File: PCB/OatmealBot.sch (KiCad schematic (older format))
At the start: 32 parts, among them J1 TerminalBlock_5pin_3.5mm, J10 ServoHeader3, J2 RPi_GPIO, J3 TerminalBlock_5pin_3.5mm, J4 ServoHeader1, J5 Motor 3, J6 Motor 4, J7 ServoHeader2, J8 Motor 1, J9 Motor 2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

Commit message: Created symbol for TB6612FNG motor driver. Added first motor driver and hooked it up.
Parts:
- removed J1, J3: TerminalBlock_5pin_3.5mm, symbol TerminalBlock_5pin_3.5mm
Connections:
- wire segments 176 -> 191
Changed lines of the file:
@@
-	-1   0    0    -1
-$EndComp
-$Comp
-L TerminalBlock_5pin_3.5mm J1
-U 1 1 5B1F55DC
-P 1000 2050
-F 0 "J1" H 1000 1750 60  0000 C CNN
-F 1 "TerminalBlock_5pin_3.5mm" H 1000 1650 60  0000 C CNN
-F 2 "" H 1000 2050 60  0001 C CNN
-F 3 "" H 1000 2050 60  0001 C CNN
-	1    1000 2050
-	0    1    1    0
-$EndComp
-$Comp
-L GND #PWR01
-U 1 1 5B1F569E
-P 1600 2050
-F 0 "#PWR01" H 1600 1800 50  0001 C CNN
-F 1 "GND" H 1600 1900 50  0000 C CNN
-F 2 "" H 1600 2050 50  0000 C CNN
-F 3 "" H 1600 2050 50  0000 C CNN
-	1    1600 2050
 	-1   0    0    -1
 $EndComp
@@
 	-1   0    0    -1
 $EndComp
-Text GLabel 1600 2750 0    60   Input ~ 0
+Text GLabel 1700 2750 0    60   Input ~ 0
 +5V
 $Comp
@@
 	1750 2600 1650 2600
 Wire Wire Line
-	1750 2750 1600 2750
-Wire Wire Line
-	1200 2050 1600 2050
-Wire Wire Line
-	1200 1850 1200 1100
-Wire Wire Line
-	1200 1100 1750 1100
-Wire Wire Line
-	1200 1950 1300 1950
-Wire Wire Line
-	1300 1950 1300 1250
-Wire Wire Line
-	1300 1250 1750 1250
-Wire Wire Line
-	1200 2150 1400 2150
-Wire Wire Line
-	1400 2150 1400 2300
-Wire Wire Line
-	1400 2300 1750 2300
-Wire Wire Line
-	1200 2250 1300 2250
-Wire Wire Line
-	1300 2250 1300 2450
-Wire Wire Line
-	1300 2450 1750 2450
-$Comp
-L TerminalBlock_5pin_3.5mm J3
-U 1 1 5B2052F2
-P 1000 4650
-F 0 "J3" H 1000 4350 60  0000 C CNN
-F 1 "TerminalBlock_5pin_3.5mm" H 1000 4250 60  0000 C CNN
-F 2 "" H 1000 4650 60  0001 C CNN
-F 3 "" H 1000 4650 60  0001 C CNN
-	1    1000 4650
-	0    1    1    0
-$EndComp
-Wire Wire Line
-	1200 4450 1200 3750
+	1750 2750 1700 2750
+Wire Wire Line
+	1100 1100 1750 1100
+Wire Wire Line
+	1200 1250 1750 1250
+Wire Wire Line
+	1300 2300 1750 2300
 Wire Wire Line
 	1200 3750 1700 3750
 Wire Wire Line
-	1200 4550 1300 4550
-Wire Wire Line
-	1300 4550 1300 3900
-Wire Wire Line
 	1300 3900 1700 3900
-$Comp
-L GND #PWR04
-U 1 1 5B20544B
-P 1400 4650
-F 0 "#PWR04" H 1400 4400 50  0001 C CNN
-F 1 "GND" H 1400 4500 50  0000 C CNN
-F 2 "" H 1400 4650 50  0000 C CNN
-F 3 "" H 1400 4650 50  0000 C CNN
-	1    1400 4650
-	1    0    0    -1
-$EndComp
 $Comp
 L GND #PWR05
@@
 	1700 4050 1600 4050
 Wire Wire Line
-	1200 4650 1400 4650
-Wire Wire Line
 	1600 5300 1700 5300
 Text GLabel 1550 5450 0    60   Input ~ 0
@@
 	1700 5450 1550 5450
 Wire Wire Line
-	1200 4750 1300 4750
-Wire Wire Line
-	1300 4750 1300 5000
-Wire Wire Line
 	1300 5000 1700 5000
-Wire Wire Line
-	1200 4850 1200 5150
 Wire Wire Line
 	1200 5150 1700 5150
@@
 	4000 2650 4000 2550
 Wire Wire Line
-	3850 2550 4250 2550
+	3850 2550 4000 2550
+Wire Wire Line
+	4000 2550 4250 2550
 Wire Wire Line
 	3850 2650 3850 2550
 Connection ~ 4000 2550
 Wire Wire Line
-	3500 2350 3500 2650
+	3500 2350 3500 2550
+Wire Wire Line
+	3500 2550 3500 2650
 Wire Wire Line
 	3650 2650 3650 2550
@@
 	1700 4500 1700 4650
 Wire Wire Line
-	1700 4650 3000 4650
-Wire Wire Line
-	3000 4650 3000 3550
-Wire Wire Line
-	3000 3550 3250 3550
+	1700 4650 2950 4650
+Wire Wire Line
+	2950 4650 2950 3550
+Wire Wire Line
+	2950 3550 3250 3550
 Wire Wire Line
 	1700 4350 1600 4350
@@
 	1600 4350 1600 4750
 Wire Wire Line
-	1600 4750 3100 4750
-Wire Wire Line
-	3100 4750 3100 3650
-Wire Wire Line
-	3100 3650 3250 3650
+	1600 4750 3050 4750
+Wire Wire Line
+	3050 4750 3050 3650
+Wire Wire Line
+	3050 3650 3250 3650
 Wire Wire Line
 	3150 6000 3150 3750
@@
 	1050 7150 1050 6550
 Wire Wire Line
-	600  6550 5550 6550
+	600  6550 1050 6550
+Wire Wire Line
+	1050 6550 1800 6550
+Wire Wire Line
+	1800 6550 2550 6550
+Wire Wire Line
+	2550 6550 3300 6550
+Wire Wire Line
+	3300 6550 4050 6550
+Wire Wire Line
+	4050 6550 4800 6550
+Wire Wire Line
+	4800 6550 5550 6550
 Wire Wire Line
 	1800 6550 1800 7150
@@
 +5V
 Wire Wire Line
-	1250 6250 1250 7150
-Wire Wire Line
-	1250 6400 5750 6400
+	1250 6250 1250 6400
+Wire Wire Line
+	1250 6400 1250 7150
+Wire Wire Line
+	1250 6400 2000 6400
+Wire Wire Line
+	2000 6400 2750 6400
+Wire Wire Line
+	2750 6400 3500 6400
+Wire Wire Line
+	3500 6400 4250 6400
+Wire Wire Line
+	4250 6400 5000 6400
+Wire Wire Line
+	5000 6400 5750 6400
 Wire Wire Line
 	2000 6400 2000 7150
@@
 	7900 2650 8000 2650
 Wire Wire Line
-	8000 2450 8000 2750
+	8000 2450 8000 2650
+Wire Wire Line
+	8000 2650 8000 2750
 Wire Wire Line
 	8000 2750 7900 2750
@@
 $EndComp
 Wire Wire Line
-	4650 1900 4650 2100
-Wire Wire Line
-	3900 1700 4350 1700
-Wire Wire Line
-	4100 2000 4950 2000
+	4650 1900 4650 2000
+Wire Wire Line
+	4650 2000 4650 2100
+Wire Wire Line
+	3900 1700 4100 1700
+Wire Wire Line
+	4100 1700 4350 1700
+Wire Wire Line
+	4100 2000 4650 2000
+Wire Wire Line
+	4650 2000 4950 2000
 Connection ~ 4650 2000
 Text GLabel 5850 2950 0    60   Output ~ 0
@@
 $EndComp
 Wire Wire Line
-	4600 1000 4600 1200
-Wire Wire Line
-	4100 1100 4900 1100
+	4600 1000 4600 1100
+Wire Wire Line
+	4600 1100 4600 1200
+Wire Wire Line
+	4100 1100 4600 1100
+Wire Wire Line
+	4600 1100 4900 1100
 Connection ~ 4600 1100
 Wire Wire Line
@@
 	4900 600  4600 600
 Wire Wire Line
-	3900 800  4300 800
+	3900 800  4100 800
+Wire Wire Line
+	4100 800  4300 800
 Text GLabel 3900 800  0    60   Input ~ 0
 HighPower2
@@
 	6000 2850 5850 2850
 Wire Wire Line
-	8650 6250 8950 6250
+	8650 6250 8800 6250
+Wire Wire Line
+	8800 6250 8950 6250
 Wire Wire Line
 	8800 6100 8800 6250
@@
 	5200 7150 5200 7000
 $Sheet
-S 3900 5050 1250 500
+S 550  2600 500  1750
 U 5B4A79AB
 F0 "MotorController" 60
 F1 "OatmealBoxMotorController.sch" 60
+F2 "Motor1+" I R 1050 2700 60
+F3 "Motor1-" I R 1050 2850 60
+F4 "Motor2+" I R 1050 3000 60
+F5 "Motor2-" I R 1050 3150 60
 $EndSheet
+Wire Wire Line
+	1050 2700 1100 2700
+Wire Wire Line
+	1100 2700 1100 1100
+Wire Wire Line
+	1200 1250 1200 2850
+Wire Wire Line
+	1200 2850 1050 2850
+Wire Wire Line
+	1300 2300 1300 3000
+Wire Wire Line
+	1300 3000 1050 3000
+Wire Wire Line
+	1750 2450 1400 2450
+Wire Wire Line
+	1400 2450 1400 3150
+Wire Wire Line
+	1400 3150 1050 3150
 $EndSCHEMATC

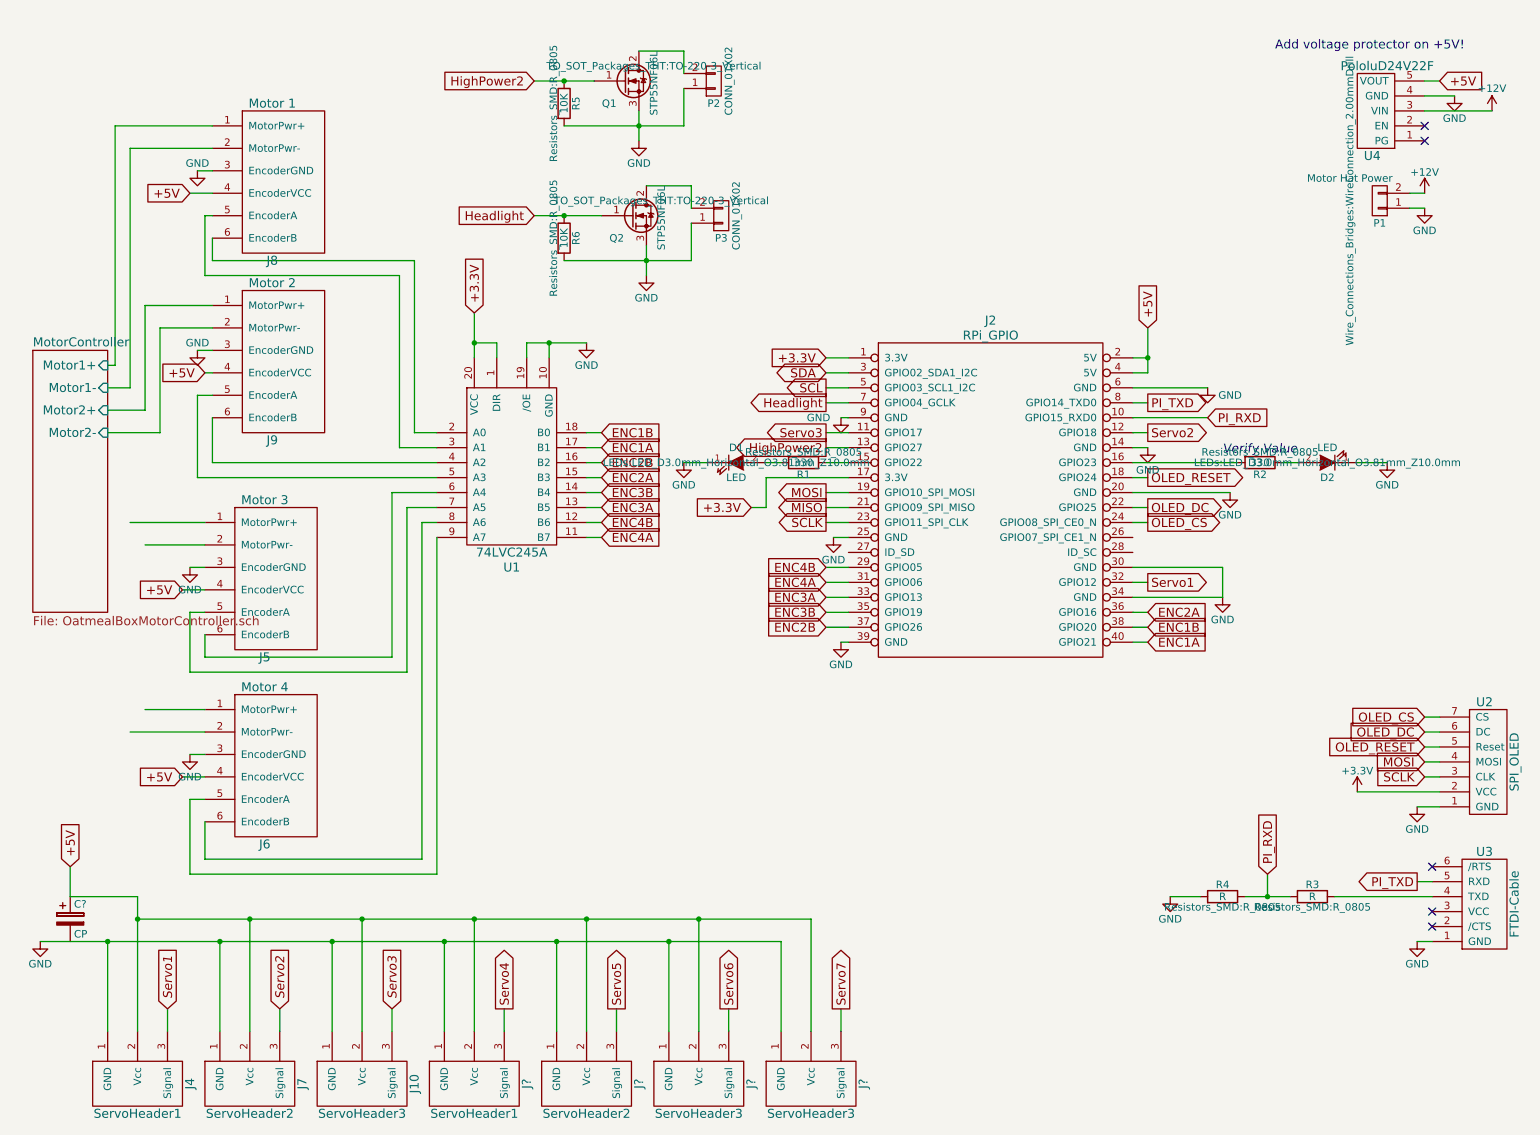
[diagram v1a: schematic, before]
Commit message: Added second motor driver. Got everything hooked up back.
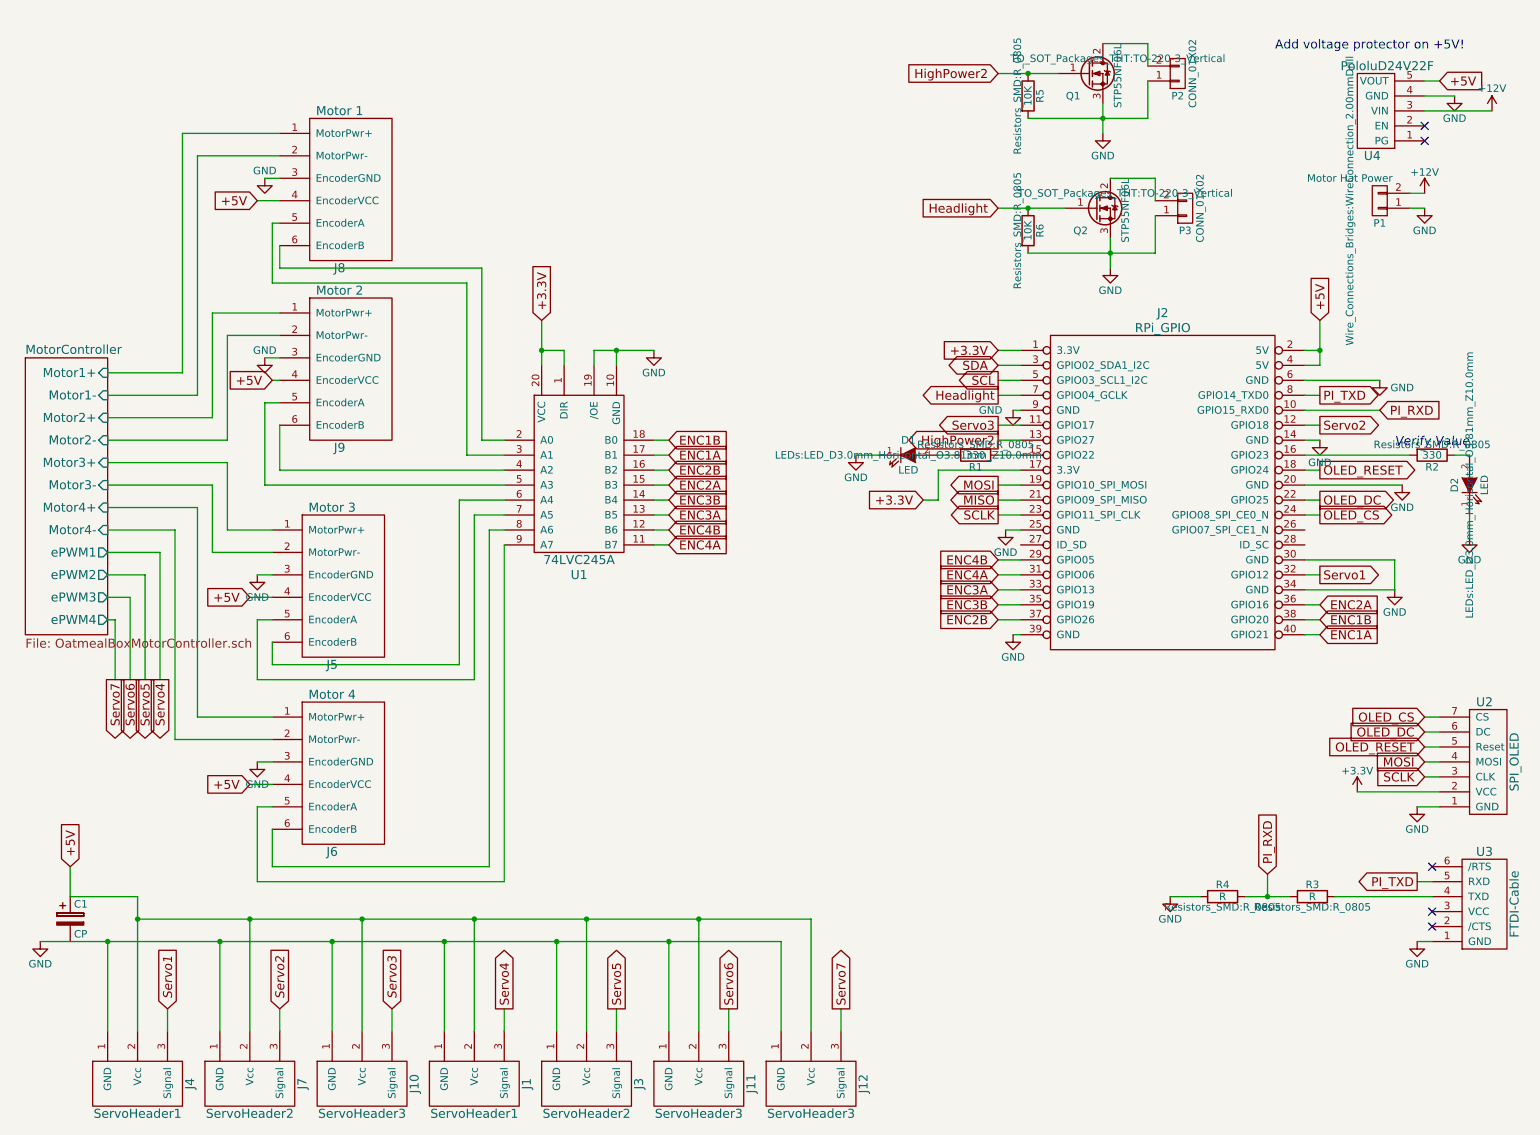
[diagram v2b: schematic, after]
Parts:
- gave numbers to parts that had none: 5
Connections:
- net MotorController/Motor3+: now reaches J5.1 (MotorPwr+)
- net MotorController/Motor3-: now reaches J5.2 (MotorPwr-)
- net MotorController/Motor4+: now reaches J6.1 (MotorPwr+)
- net MotorController/Motor4-: now reaches J6.2 (MotorPwr-)
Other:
- moved on the sheet: D1, D2, J2, J5, J6, J8, J9, P2, P3, Q1, Q2, R1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

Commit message: Connected I2C, fixed ERC errors
Connected I2C to the PWM controller.
Fixed ERC errors.
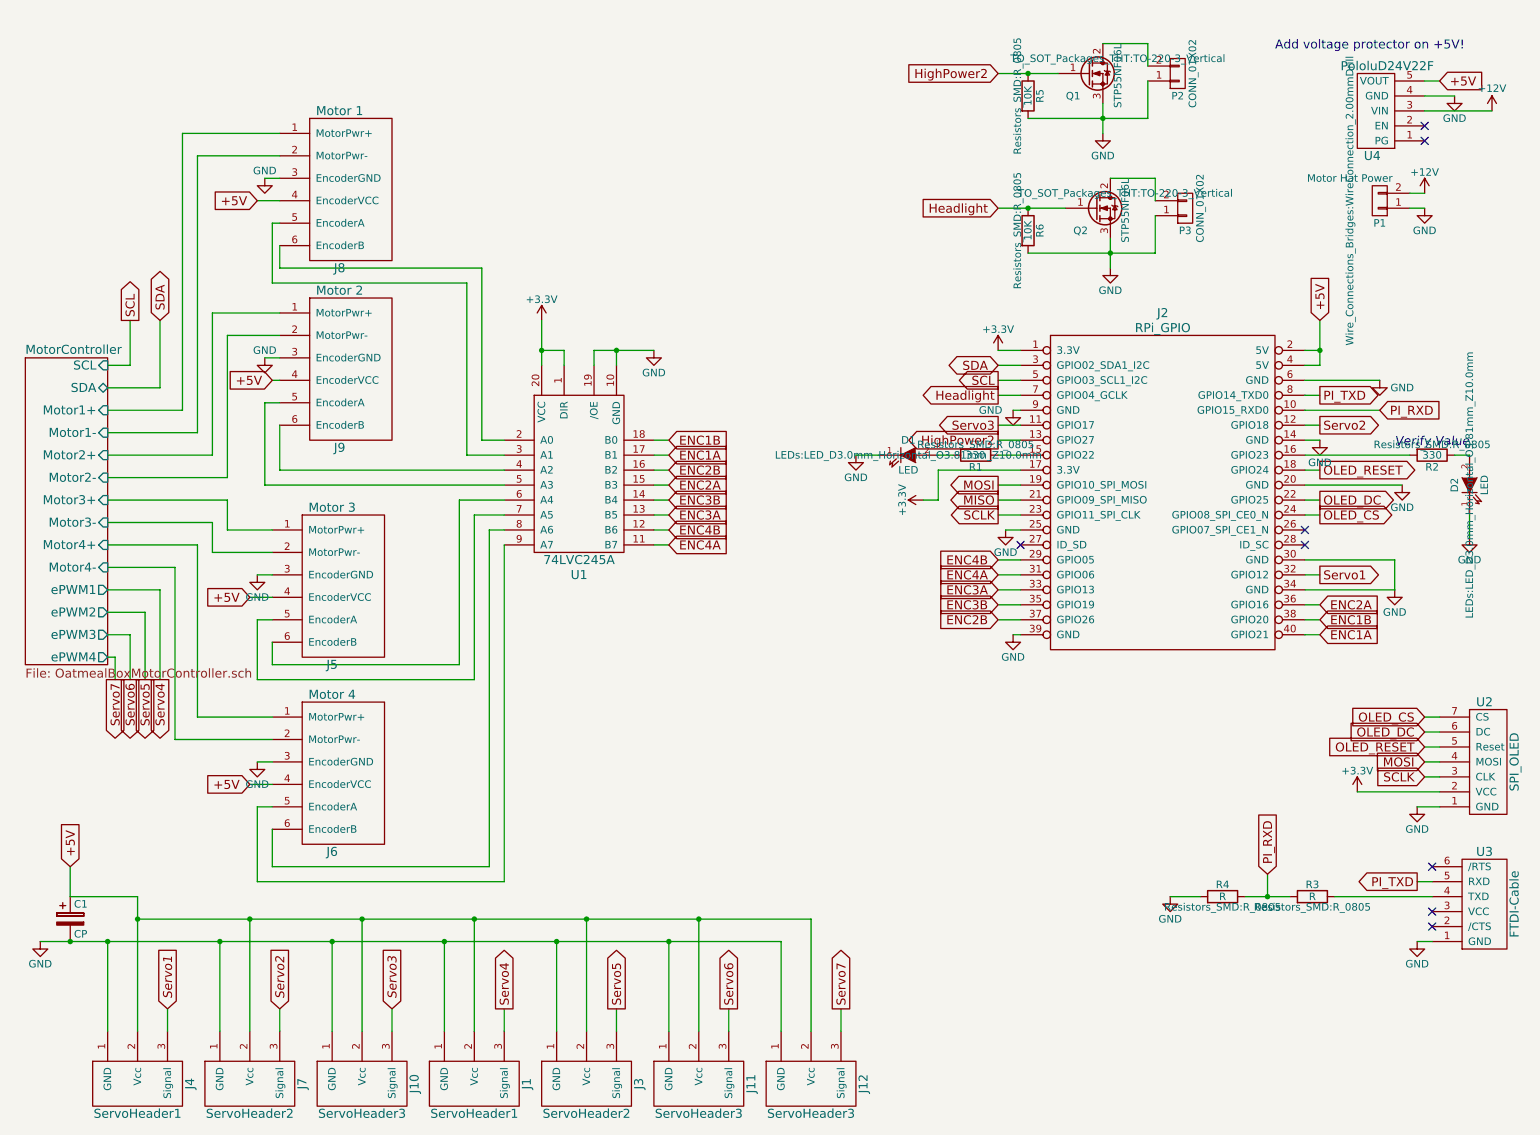
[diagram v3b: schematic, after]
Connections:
- net +3.3V is gone; now on net +3V3: J2.1 (3.3V), J2.17 (3.3V), U1.1 (DIR), U1.20 (VCC)
- net GND: now also C1.2
- no-connect marks 5 -> 8
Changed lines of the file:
@@
 	1    0    0    -1
 $EndComp
-Text GLabel 3950 2400 1    60   Input ~ 0
-+3.3V
 $Comp
 L GND #PWR05
@@
 Wire Wire Line
 	9150 3700 9050 3700
-Text GLabel 7000 2600 0    60   Input ~ 0
-+3.3V
 Wire Wire Line
 	7150 2600 7000 2600
@@
 	7150 3200 7000 3200
 Connection ~ 7200 750
-Text GLabel 6500 3600 0    60   Input ~ 0
-+3.3V
 Wire Wire Line
 	7150 3400 6600 3400
@@
 	5200 7150 5200 7000
 $Sheet
-S 500  2650 550  1850
+S 500  2650 550  2050
 U 5B4A79AB
 F0 "MotorController" 60
 F1 "OatmealBoxMotorController.sch" 60
-F2 "Motor1+" I R 1050 2750 60
-F3 "Motor1-" I R 1050 2900 60
-F4 "Motor2+" I R 1050 3050 60
-F5 "Motor2-" I R 1050 3200 60
-F6 "Motor3+" I R 1050 3350 60
-F7 "Motor3-" I R 1050 3500 60
-F8 "Motor4+" I R 1050 3650 60
-F9 "Motor4-" I R 1050 3800 60
-F10 "ePWM1" O R 1050 3950 60
-F11 "ePWM2" O R 1050 4100 60
-F12 "ePWM3" O R 1050 4250 60
-F13 "ePWM4" O R 1050 4400 60
+F2 "Motor1+" I R 1050 3000 60
+F3 "Motor1-" I R 1050 3150 60
+F4 "Motor2+" I R 1050 3300 60
+F5 "Motor2-" I R 1050 3450 60
+F6 "Motor3+" I R 1050 3600 60
+F7 "Motor3-" I R 1050 3750 60
+F8 "Motor4+" I R 1050 3900 60
+F9 "Motor4-" I R 1050 4050 60
+F10 "ePWM1" O R 1050 4200 60
+F11 "ePWM2" O R 1050 4350 60
+F12 "ePWM3" O R 1050 4500 60
+F13 "ePWM4" O R 1050 4650 60
+F14 "SDA" B R 1050 2850 60
+F15 "SCL" I R 1050 2700 60
 $EndSheet
 Wire Wire Line
-	1650 1300 1650 2900
-Wire Wire Line
-	1650 2900 1050 2900
-Wire Wire Line
-	1750 2350 1750 3050
-Wire Wire Line
-	1750 3050 1050 3050
+	1650 1300 1650 3150
+Wire Wire Line
+	1650 3150 1050 3150
+Wire Wire Line
+	1750 2350 1750 3300
+Wire Wire Line
+	1750 3300 1050 3300
 Wire Wire Line
 	2200 2500 1850 2500
 Wire Wire Line
-	1850 2500 1850 3200
-Wire Wire Line
-	1850 3200 1050 3200
+	1850 2500 1850 3450
+Wire Wire Line
+	1850 3450 1050 3450
 Wire Wire Line
 	10150 3700 10150 3850
 Wire Wire Line
-	1550 1150 1550 2750
-Wire Wire Line
-	1550 2750 1050 2750
+	1550 1150 1550 3000
+Wire Wire Line
+	1550 3000 1050 3000
 Wire Wire Line
 	2150 3800 1850 3800
 Wire Wire Line
-	1850 3800 1850 3350
-Wire Wire Line
-	1850 3350 1050 3350
+	1850 3800 1850 3600
+Wire Wire Line
+	1850 3600 1050 3600
 Wire Wire Line
 	2150 3950 1750 3950
 Wire Wire Line
-	1750 3950 1750 3500
-Wire Wire Line
-	1750 3500 1050 3500
+	1750 3950 1750 3750
+Wire Wire Line
+	1750 3750 1050 3750
 Wire Wire Line
 	2150 5050 1650 5050
 Wire Wire Line
-	1650 5050 1650 3650
-Wire Wire Line
-	1650 3650 1050 3650
+	1650 5050 1650 3900
+Wire Wire Line
+	1650 3900 1050 3900
 Wire Wire Line
 	2150 5200 1500 5200
 Wire Wire Line
-	1500 5200 1500 3800
-Wire Wire Line
-	1500 3800 1050 3800
+	1500 5200 1500 4050
+Wire Wire Line
+	1500 4050 1050 4050
 Text GLabel 1400 4800 3    60   Output ~ 0
 Servo4
@@
 Servo7
 Wire Wire Line
-	1050 4400 1100 4400
-Wire Wire Line
-	1050 4250 1200 4250
-Wire Wire Line
-	1050 4100 1300 4100
-Wire Wire Line
-	1050 3950 1400 3950
-Wire Wire Line
-	1400 3950 1400 4800
-Wire Wire Line
-	1300 4100 1300 4800
-Wire Wire Line
-	1200 4250 1200 4800
-Wire Wire Line
-	1100 4400 1100 4800
+	1050 4500 1200 4500
+Wire Wire Line
+	1050 4350 1300 4350
+Wire Wire Line
+	1050 4200 1400 4200
+Wire Wire Line
+	1400 4200 1400 4800
+Wire Wire Line
+	1300 4350 1300 4800
+Wire Wire Line
+	1200 4500 1200 4800
+$Comp
+L +3.3V #PWR026
+U 1 1 5B4FAF00
+P 7000 2600
+F 0 "#PWR026" H 7000 2450 50  0001 C CNN
+F 1 "+3.3V" H 7000 2740 50  0000 C CNN
+F 2 "" H 7000 2600 50  0001 C CNN
+F 3 "" H 7000 2600 50  0001 C CNN
+	1    7000 2600
+	1    0    0    -1
+$EndComp
+Wire Wire Line
+	1100 4800 1100 4650
+Wire Wire Line
+	1100 4650 1050 4650
+Text GLabel 1200 2400 1    60   Output ~ 0
+SCL
+Text GLabel 1400 2400 1    60   BiDi ~ 0
+SDA
+Wire Wire Line
+	1200 2400 1200 2700
+Wire Wire Line
+	1200 2700 1050 2700
+Wire Wire Line
+	1050 2850 1400 2850
+Wire Wire Line
+	1400 2850 1400 2400
+$Comp
+L +3.3V #PWR027
+U 1 1 5B503843
+P 3950 2400
+F 0 "#PWR027" H 3950 2250 50  0001 C CNN
+F 1 "+3.3V" H 3950 2540 50  0000 C CNN
+F 2 "" H 3950 2400 50  0001 C CNN
+F 3 "" H 3950 2400 50  0001 C CNN
+	1    3950 2400
+	1    0    0    -1
+$EndComp
+NoConn ~ 7150 3900
+NoConn ~ 9050 3900
+NoConn ~ 9050 3800
+$Comp
+L +3.3V #PWR028
+U 1 1 5B5043F5
+P 6500 3600
+F 0 "#PWR028" H 6500 3450 50  0001 C CNN
+F 1 "+3.3V" H 6500 3740 50  0000 C CNN
+F 2 "" H 6500 3600 50  0001 C CNN
+F 3 "" H 6500 3600 50  0001 C CNN
+	1    6500 3600
+	0    -1   -1   0
+$EndComp
+Connection ~ 800  6550
 $EndSCHEMATC
